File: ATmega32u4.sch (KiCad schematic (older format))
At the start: 33 parts, among them J1 USB_B_Mini, J2 AVR-ISP-6, SW70 SW_Push, U1 ATmega32U4-MU, Y1 16MHz

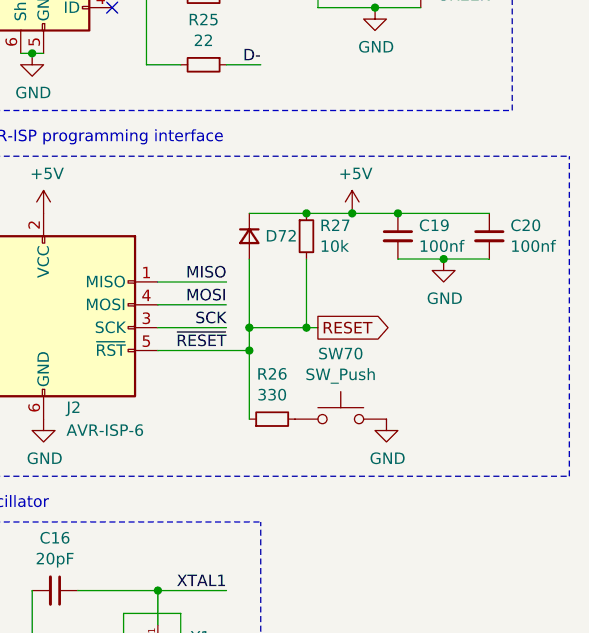
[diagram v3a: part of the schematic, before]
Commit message: All buttons moved to new layout
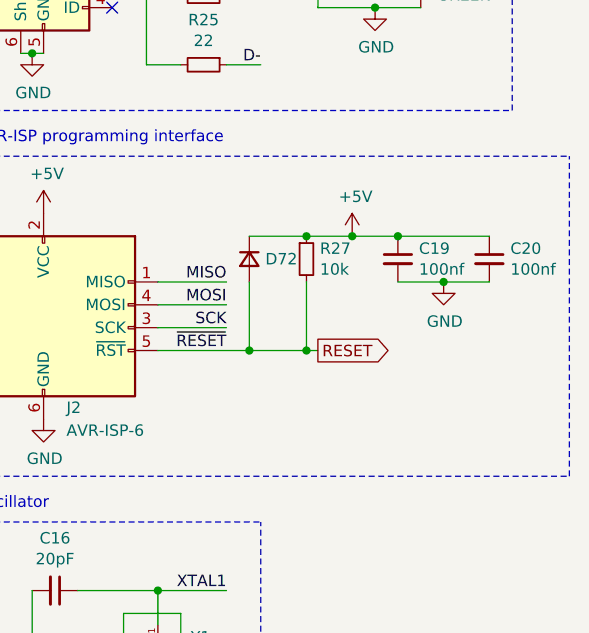
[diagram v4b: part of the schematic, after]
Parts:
- removed R26: 330, Collins-FMS-3000:Perfect_0402, symbol Device:R_Small
- removed SW70: SW_Push, Button_Switch_THT:SW_PUSH_6mm_H4.3mm, symbol Switch:SW_Push
- J2: footprint Connector_PinHeader_2.54mm:PinHeader_2x03_P2.54mm_Vertical -> Connector:Tag-Connect_TC2030-IDC-NL_2x03_P1.27mm_Vertical
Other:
- moved on the sheet: C19, C20, D72, R27
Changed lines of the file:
@@
 	3950 2050 3950 3450
 Wire Wire Line
-	5600 2300 5800 2300
-Connection ~ 5600 2300
+	5600 2400 5800 2400
+Connection ~ 5600 2400
 $Comp
 L power:+5V #PWR?
 U 1 1 61F97F3E
-P 5600 2300
+P 5600 2400
 AR Path="/61F97F3E" Ref="#PWR?"  Part="1"
 AR Path="/61F7F1B9/61F97F3E" Ref="#PWR0126"  Part="1"
-F 0 "#PWR0126" H 5600 2150 50  0001 C CNN
-F 1 "+5V" H 5615 2473 50  0000 C CNN
-F 2 "" H 5600 2300 50  0001 C CNN
-F 3 "" H 5600 2300 50  0001 C CNN
-	1    5600 2300
-	1    0    0    -1
-$EndComp
-Wire Wire Line
-	6000 2500 6200 2500
-Connection ~ 6000 2500
+F 0 "#PWR0126" H 5600 2250 50  0001 C CNN
+F 1 "+5V" H 5615 2573 50  0000 C CNN
+F 2 "" H 5600 2400 50  0001 C CNN
+F 3 "" H 5600 2400 50  0001 C CNN
+	1    5600 2400
+	1    0    0    -1
+$EndComp
+Wire Wire Line
+	6000 2600 6200 2600
+Connection ~ 6000 2600
 $Comp
 L power:GND #PWR?
 U 1 1 61F97F46
-P 6000 2500
+P 6000 2600
 AR Path="/61F97F46" Ref="#PWR?"  Part="1"
 AR Path="/61F7F1B9/61F97F46" Ref="#PWR0127"  Part="1"
-F 0 "#PWR0127" H 6000 2250 50  0001 C CNN
-F 1 "GND" H 6005 2327 50  0000 C CNN
-F 2 "" H 6000 2500 50  0001 C CNN
-F 3 "" H 6000 2500 50  0001 C CNN
-	1    6000 2500
-	1    0    0    -1
-$EndComp
-Wire Wire Line
-	5800 2500 6000 2500
-Wire Wire Line
-	5800 2300 6200 2300
+F 0 "#PWR0127" H 6000 2350 50  0001 C CNN
+F 1 "GND" H 6005 2427 50  0000 C CNN
+F 2 "" H 6000 2600 50  0001 C CNN
+F 3 "" H 6000 2600 50  0001 C CNN
+	1    6000 2600
+	1    0    0    -1
+$EndComp
+Wire Wire Line
+	5800 2600 6000 2600
+Wire Wire Line
+	5800 2400 6200 2400
 $Comp
 L Device:C_Small C?
 U 1 1 61F97F4E
-P 6200 2400
+P 6200 2500
 AR Path="/61F97F4E" Ref="C?"  Part="1"
 AR Path="/61F7F1B9/61F97F4E" Ref="C20"  Part="1"
-F 0 "C20" H 6292 2446 50  0000 L CNN
-F 1 "100nf" H 6292 2355 50  0000 L CNN
-F 2 "Collins-FMS-3000:Perfect_0402" H 6200 2400 50  0001 C CNN
-F 3 "~" H 6200 2400 50  0001 C CNN
-F 4 "0402" H 6200 2400 50  0001 C CNN "JLC"
-F 5 "C1525" H 6200 2400 50  0001 C CNN "LCSC"
-	1    6200 2400
-	1    0    0    -1
-$EndComp
-Connection ~ 5800 2300
+F 0 "C20" H 6292 2546 50  0000 L CNN
+F 1 "100nf" H 6292 2455 50  0000 L CNN
+F 2 "Collins-FMS-3000:Perfect_0402" H 6200 2500 50  0001 C CNN
+F 3 "~" H 6200 2500 50  0001 C CNN
+F 4 "0402" H 6200 2500 50  0001 C CNN "JLC"
+F 5 "C1525" H 6200 2500 50  0001 C CNN "LCSC"
+	1    6200 2500
+	1    0    0    -1
+$EndComp
+Connection ~ 5800 2400
 $Comp
 L Device:C_Small C?
 U 1 1 61F97F55
-P 5800 2400
+P 5800 2500
 AR Path="/61F97F55" Ref="C?"  Part="1"
 AR Path="/61F7F1B9/61F97F55" Ref="C19"  Part="1"
-F 0 "C19" H 5892 2446 50  0000 L CNN
-F 1 "100nf" H 5892 2355 50  0000 L CNN
-F 2 "Collins-FMS-3000:Perfect_0402" H 5800 2400 50  0001 C CNN
-F 3 "~" H 5800 2400 50  0001 C CNN
-F 4 "0402" H 5800 2400 50  0001 C CNN "JLC"
-F 5 "C1525" H 5800 2400 50  0001 C CNN "LCSC"
-	1    5800 2400
-	1    0    0    -1
-$EndComp
-Wire Wire Line
-	5400 2300 5600 2300
-Connection ~ 5400 2300
-Wire Wire Line
-	5150 2300 5400 2300
-Connection ~ 5400 2800
-Wire Wire Line
-	5450 2800 5400 2800
-Text GLabel 5450 2800 2    50   Output ~ 0
+F 0 "C19" H 5892 2546 50  0000 L CNN
+F 1 "100nf" H 5892 2455 50  0000 L CNN
+F 2 "Collins-FMS-3000:Perfect_0402" H 5800 2500 50  0001 C CNN
+F 3 "~" H 5800 2500 50  0001 C CNN
+F 4 "0402" H 5800 2500 50  0001 C CNN "JLC"
+F 5 "C1525" H 5800 2500 50  0001 C CNN "LCSC"
+	1    5800 2500
+	1    0    0    -1
+$EndComp
+Wire Wire Line
+	5400 2400 5600 2400
+Connection ~ 5400 2400
+Wire Wire Line
+	5150 2400 5400 2400
+Connection ~ 5400 2900
+Wire Wire Line
+	5450 2900 5400 2900
+Text GLabel 5450 2900 2    50   Output ~ 0
 RESET
 Wire Wire Line
-	5400 2800 5400 2500
+	5400 2900 5400 2600
 $Comp
 L Device:R_Small R?
 U 1 1 61F97F62
-P 5400 2400
+P 5400 2500
 AR Path="/61F97F62" Ref="R?"  Part="1"
 AR Path="/61F7F1B9/61F97F62" Ref="R27"  Part="1"
-F 0 "R27" H 5459 2446 50  0000 L CNN
-F 1 "10k" H 5459 2355 50  0000 L CNN
-F 2 "Collins-FMS-3000:Perfect_0402" H 5400 2400 50  0001 C CNN
-F 3 "~" H 5400 2400 50  0001 C CNN
-F 4 "0402" H 5400 2400 50  0001 C CNN "JLC"
-F 5 "C25744" H 5400 2400 50  0001 C CNN "LCSC"
-	1    5400 2400
-	1    0    0    -1
-$EndComp
-Wire Wire Line
-	5150 2800 5150 2500
-Connection ~ 5150 2800
-Wire Wire Line
-	5150 2800 5400 2800
-Connection ~ 5150 2900
-Wire Wire Line
-	5150 2900 5150 3200
-Wire Wire Line
-	4750 2900 5150 2900
-Wire Wire Line
-	5150 2900 5150 2800
-$Comp
-L power:GND #PWR?
-U 1 1 61F97F6F
-P 5750 3200
-AR Path="/61F97F6F" Ref="#PWR?"  Part="1"
-AR Path="/61F7F1B9/61F97F6F" Ref="#PWR0128"  Part="1"
-F 0 "#PWR0128" H 5750 2950 50  0001 C CNN
-F 1 "GND" H 5755 3027 50  0000 C CNN
-F 2 "" H 5750 3200 50  0001 C CNN
-F 3 "" H 5750 3200 50  0001 C CNN
-	1    5750 3200
-	1    0    0    -1
-$EndComp
-$Comp
-L Switch:SW_Push SW?
-U 1 1 61F97F75
-P 5550 3200
-AR Path="/61F97F75" Ref="SW?"  Part="1"
-AR Path="/61F7F1B9/61F97F75" Ref="SW70"  Part="1"
-F 0 "SW70" H 5550 3485 50  0000 C CNN
-F 1 "SW_Push" H 5550 3394 50  0000 C CNN
-F 2 "Button_Switch_THT:SW_PUSH_6mm_H4.3mm" H 5550 3400 50  0001 C CNN
-F 3 "~" H 5550 3400 50  0001 C CNN
-	1    5550 3200
-	1    0    0    -1
-$EndComp
-$Comp
-L Device:R_Small R?
-U 1 1 61F97F7B
-P 5250 3200
-AR Path="/61F97F7B" Ref="R?"  Part="1"
-AR Path="/61F7F1B9/61F97F7B" Ref="R26"  Part="1"
-F 0 "R26" V 5446 3200 50  0000 C CNN
-F 1 "330" V 5355 3200 50  0000 C CNN
-F 2 "Collins-FMS-3000:Perfect_0402" H 5250 3200 50  0001 C CNN
-F 3 "~" H 5250 3200 50  0001 C CNN
-F 4 "0402" H 5250 3200 50  0001 C CNN "JLC"
-F 5 "C25104" H 5250 3200 50  0001 C CNN "LCSC"
-	1    5250 3200
-	0    -1   -1   0
+F 0 "R27" H 5459 2546 50  0000 L CNN
+F 1 "10k" H 5459 2455 50  0000 L CNN
+F 2 "Collins-FMS-3000:Perfect_0402" H 5400 2500 50  0001 C CNN
+F 3 "~" H 5400 2500 50  0001 C CNN
+F 4 "0402" H 5400 2500 50  0001 C CNN "JLC"
+F 5 "C25744" H 5400 2500 50  0001 C CNN "LCSC"
+	1    5400 2500
+	1    0    0    -1
 $EndComp
 $Comp
 L Device:D_Small D?
 U 1 1 61F97F81
-P 5150 2400
+P 5150 2500
 AR Path="/61F97F81" Ref="D?"  Part="1"
 AR Path="/61F7F1B9/61F97F81" Ref="D72"  Part="1"
-F 0 "D72" V 5150 2470 50  0000 L CNN
-F 1 "D_Small" V 5195 2470 50  0001 L CNN
-F 2 "Diode_SMD:D_SOD-323F" V 5150 2400 50  0001 C CNN
-F 3 "~" V 5150 2400 50  0001 C CNN
-F 4 "SOD-323F" H 5150 2400 50  0001 C CNN "JLC"
-F 5 "C2128" H 5150 2400 50  0001 C CNN "LCSC"
-	1    5150 2400
+F 0 "D72" V 5150 2570 50  0000 L CNN
+F 1 "D_Small" V 5195 2570 50  0001 L CNN
+F 2 "Diode_SMD:D_SOD-323F" V 5150 2500 50  0001 C CNN
+F 3 "~" V 5150 2500 50  0001 C CNN
+F 4 "SOD-323F" H 5150 2500 50  0001 C CNN "JLC"
+F 5 "C2128" H 5150 2500 50  0001 C CNN "LCSC"
+	1    5150 2500
 	0    1    1    0
 $EndComp
@@
 F 0 "J2" H 4350 2450 50  0000 L CNN
 F 1 "AVR-ISP-6" H 4350 2350 50  0000 L CNN
-F 2 "Connector_PinHeader_2.54mm:PinHeader_2x03_P2.54mm_Vertical" V 4100 2850 50  0001 C CNN
+F 2 "Connector:Tag-Connect_TC2030-IDC-NL_2x03_P1.27mm_Vertical" V 4100 2850 50  0001 C CNN
 F 3 " ~" H 3075 2250 50  0001 C CNN
 	1    4350 2800
@@
 Text HLabel 3200 3000 2    50   Input ~ 0
 ROW_INTB
+Wire Wire Line
+	4750 2900 5150 2900
+Wire Wire Line
+	5150 2600 5150 2900
+Connection ~ 5150 2900
+Wire Wire Line
+	5150 2900 5400 2900
 $EndSCHEMATC

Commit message: More trace routing
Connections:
- net ROW_INTB: no longer names the net of U1.21 (PD3)
- no-connect marks 15 -> 16
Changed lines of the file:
@@
 Connection ~ 3150 3100
-Wire Wire Line
-	2400 3000 3200 3000
-Text HLabel 3200 3000 2    50   Input ~ 0
-ROW_INTB
 Wire Wire Line
 	4750 2900 5150 2900
@@
 Wire Wire Line
 	5150 2900 5400 2900
+NoConn ~ 2400 3000
 $EndSCHEMATC

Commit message: Update components to match JLCPCB availability
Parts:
- C10, C18: footprint Collins-FMS-3000:Perfect_0402 -> Capacitor_SMD:C_0603_1608Metric; JLC 0402 -> 0603; LCSC C15525 -> C96446
- D71, D73: LCSC (none) -> C72043
- FB1: footprint Capacitor_SMD:C_0805_2012Metric -> Capacitor_SMD:C_0603_1608Metric; JLC 0805 -> 0603; LCSC C72043 -> C1002
- R24, R25: LCSC 0402 -> C25092
- R28: footprint Collins-FMS-3000:Perfect_0402 -> Resistor_SMD:R_0603_1608Metric
- R3: footprint Collins-FMS-3000:Perfect_0402 -> Resistor_SMD:R_0603_1608Metric; JLC 0402 -> 0603; LCSC C25741 -> C25803
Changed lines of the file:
@@
 F 0 "C10" H 892 1046 50  0000 L CNN
 F 1 "10uF" H 892 955 50  0000 L CNN
-F 2 "Collins-FMS-3000:Perfect_0402" H 800 1000 50  0001 C CNN
+F 2 "Capacitor_SMD:C_0603_1608Metric" H 800 1000 50  0001 C CNN
 F 3 "~" H 800 1000 50  0001 C CNN
-F 4 "0402" H 800 1000 50  0001 C CNN "JLC"
-F 5 "C15525" H 800 1000 50  0001 C CNN "LCSC"
+F 4 "0603" H 800 1000 50  0001 C CNN "JLC"
+F 5 "C96446" H 800 1000 50  0001 C CNN "LCSC"
 	1    800  1000
 	1    0    0    -1
@@
 F 3 "~" V 2750 3500 50  0001 C CNN
 F 4 "0603" H 2750 3500 50  0001 C CNN "JLC"
+F 5 "C72043" H 2750 3500 50  0001 C CNN "LCSC"
 	1    2750 3500
 	0    -1   -1   0
@@
 F 0 "FB1" V 4713 1000 50  0000 C CNN
 F 1 "Ferrite_Bead_Small" V 4804 1000 50  0000 C CNN
-F 2 "Capacitor_SMD:C_0805_2012Metric" V 4880 1000 50  0001 C CNN
+F 2 "Capacitor_SMD:C_0603_1608Metric" V 4880 1000 50  0001 C CNN
 F 3 "~" H 4950 1000 50  0001 C CNN
-F 4 "0805" H 4950 1000 50  0001 C CNN "JLC"
-F 5 "C72043" H 4950 1000 50  0001 C CNN "LCSC"
+F 4 "0603" H 4950 1000 50  0001 C CNN "JLC"
+F 5 "C1002" H 4950 1000 50  0001 C CNN "LCSC"
 	1    4950 1000
 	0    1    1    0
@@
 F 3 "~" H 4950 1350 50  0001 C CNN
 F 4 "0402" H 4950 1350 50  0001 C CNN "JLC"
-F 5 "0402" H 4950 1350 50  0001 C CNN "LCSC"
+F 5 "C25092" H 4950 1350 50  0001 C CNN "LCSC"
 	1    4950 1350
 	0    1    1    0
@@
 F 3 "~" H 4950 1650 50  0001 C CNN
 F 4 "0402" H 4950 1650 50  0001 C CNN "JLC"
-F 5 "0402" H 4950 1650 50  0001 C CNN "LCSC"
+F 5 "C25092" H 4950 1650 50  0001 C CNN "LCSC"
 	1    4950 1650
 	0    1    1    0
@@
 F 0 "C18" H 5542 1146 50  0000 L CNN
 F 1 "10uF" H 5542 1055 50  0000 L CNN
-F 2 "Collins-FMS-3000:Perfect_0402" H 5450 1100 50  0001 C CNN
+F 2 "Capacitor_SMD:C_0603_1608Metric" H 5450 1100 50  0001 C CNN
 F 3 "~" H 5450 1100 50  0001 C CNN
-F 4 "0402" H 5450 1100 50  0001 C CNN "JLC"
-F 5 "C15525" H 5450 1100 50  0001 C CNN "LCSC"
+F 4 "0603" H 5450 1100 50  0001 C CNN "JLC"
+F 5 "C96446" H 5450 1100 50  0001 C CNN "LCSC"
 	1    5450 1100
 	1    0    0    -1
@@
 F 0 "R28" H 5959 1146 50  0000 L CNN
 F 1 "1K" H 5959 1055 50  0000 L CNN
-F 2 "Collins-FMS-3000:Perfect_0402" H 5900 1100 50  0001 C CNN
+F 2 "Resistor_SMD:R_0603_1608Metric" H 5900 1100 50  0001 C CNN
 F 3 "~" H 5900 1100 50  0001 C CNN
 F 4 "0402" H 5900 1100 50  0001 C CNN "JLC"
@@
 F 3 "~" V 5900 1300 50  0001 C CNN
 F 4 "0603" H 5900 1300 50  0001 C CNN "JLC"
+F 5 "C72043" H 5900 1300 50  0001 C CNN "LCSC"
 	1    5900 1300
 	0    -1   -1   0
@@
 F 0 "R3" H 3209 3296 50  0000 L CNN
 F 1 "100k" H 3209 3205 50  0000 L CNN
-F 2 "Collins-FMS-3000:Perfect_0402" H 3150 3250 50  0001 C CNN
+F 2 "Resistor_SMD:R_0603_1608Metric" H 3150 3250 50  0001 C CNN
 F 3 "~" H 3150 3250 50  0001 C CNN
-F 4 "0402" H 3150 3250 50  0001 C CNN "JLC"
-F 5 "C25741" H 3150 3250 50  0001 C CNN "LCSC"
+F 4 "0603" H 3150 3250 50  0001 C CNN "JLC"
+F 5 "C25803" H 3150 3250 50  0001 C CNN "LCSC"
 	1    3150 3250
 	1    0    0    -1

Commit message: Fix JLCPCB part number for R28
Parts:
- R28: JLC 0402 -> 0603; LCSC C11702 -> C21190
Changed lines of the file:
@@
 F 2 "Resistor_SMD:R_0603_1608Metric" H 5900 1100 50  0001 C CNN
 F 3 "~" H 5900 1100 50  0001 C CNN
-F 4 "0402" H 5900 1100 50  0001 C CNN "JLC"
-F 5 "C11702" H 5900 1100 50  0001 C CNN "LCSC"
+F 4 "0603" H 5900 1100 50  0001 C CNN "JLC"
+F 5 "C21190" H 5900 1100 50  0001 C CNN "LCSC"
 	1    5900 1100
 	1    0    0    -1
